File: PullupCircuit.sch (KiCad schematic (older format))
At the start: 4 parts, among them U4 DMC2700

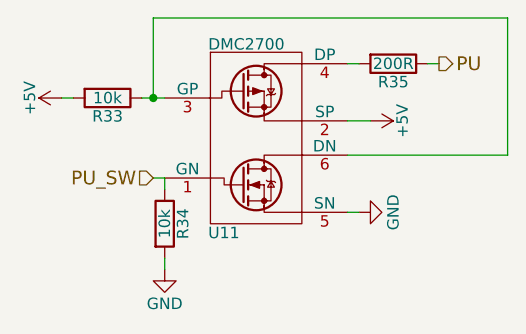
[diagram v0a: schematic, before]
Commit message: Fixed some annotations and footprints
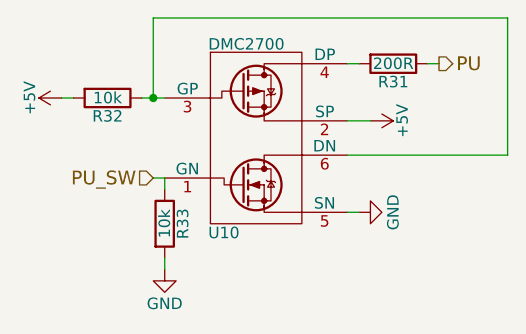
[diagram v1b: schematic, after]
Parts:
- renumbered R16 to R12, R14 to R13, R15 to R14, U4 to U3
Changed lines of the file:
@@
 $EndDescr
 $Comp
-L DMC2700 U4
+L DMC2700 U3
 U 1 1 59B3FFA1
 P 5200 2550
-AR Path="/59A988EA/59B40F2D/59B3FFA1" Ref="U4"  Part="1"
-AR Path="/59A988EA/59B419E1/59B3FFA1" Ref="U5"  Part="1"
-AR Path="/59B431E3/59B40F2D/59B3FFA1" Ref="U7"  Part="1"
-AR Path="/59B431E3/59B419E1/59B3FFA1" Ref="U8"  Part="1"
-AR Path="/59B46FD6/59B40F2D/59B3FFA1" Ref="U10"  Part="1"
-AR Path="/59B46FD6/59B419E1/59B3FFA1" Ref="U11"  Part="1"
-F 0 "U11" H 4990 2110 50  0000 L CNN
+AR Path="/59A988EA/59B40F2D/59B3FFA1" Ref="U3"  Part="1"
+AR Path="/59A988EA/59B419E1/59B3FFA1" Ref="U4"  Part="1"
+AR Path="/59B431E3/59B40F2D/59B3FFA1" Ref="U6"  Part="1"
+AR Path="/59B431E3/59B419E1/59B3FFA1" Ref="U7"  Part="1"
+AR Path="/59B46FD6/59B40F2D/59B3FFA1" Ref="U9"  Part="1"
+AR Path="/59B46FD6/59B419E1/59B3FFA1" Ref="U10"  Part="1"
+F 0 "U10" H 4990 2110 50  0000 L CNN
 F 1 "DMC2700" H 4990 2935 50  0000 L CNN
 F 2 "TO_SOT_Packages_SMD:SOT-23-6_Handsoldering" H 5450 2475 50  0001 L CIN
@@
 	5600 2500 5700 2500
 $Comp
-L R R16
+L R R12
 U 1 1 59B4002B
 P 5800 2250
-AR Path="/59A988EA/59B40F2D/59B4002B" Ref="R16"  Part="1"
-AR Path="/59A988EA/59B419E1/59B4002B" Ref="R19"  Part="1"
-AR Path="/59B431E3/59B40F2D/59B4002B" Ref="R24"  Part="1"
-AR Path="/59B431E3/59B419E1/59B4002B" Ref="R27"  Part="1"
-AR Path="/59B46FD6/59B40F2D/59B4002B" Ref="R32"  Part="1"
-AR Path="/59B46FD6/59B419E1/59B4002B" Ref="R35"  Part="1"
-F 0 "R35" V 5880 2250 50  0000 C CNN
+AR Path="/59A988EA/59B40F2D/59B4002B" Ref="R12"  Part="1"
+AR Path="/59A988EA/59B419E1/59B4002B" Ref="R15"  Part="1"
+AR Path="/59B431E3/59B40F2D/59B4002B" Ref="R20"  Part="1"
+AR Path="/59B431E3/59B419E1/59B4002B" Ref="R23"  Part="1"
+AR Path="/59B46FD6/59B40F2D/59B4002B" Ref="R28"  Part="1"
+AR Path="/59B46FD6/59B419E1/59B4002B" Ref="R31"  Part="1"
+F 0 "R31" V 5880 2250 50  0000 C CNN
 F 1 "200R" V 5800 2250 50  0000 C CNN
 F 2 "Resistors_SMD:R_1206_HandSoldering" V 5730 2250 50  0001 C CNN
@@
 	6000 2250 5950 2250
 $Comp
-L +5V #PWR044
+L +5V #PWR042
 U 1 1 59B40098
 P 5700 2500
-AR Path="/59A988EA/59B40F2D/59B40098" Ref="#PWR044"  Part="1"
-AR Path="/59A988EA/59B419E1/59B40098" Ref="#PWR048"  Part="1"
-AR Path="/59B431E3/59B40F2D/59B40098" Ref="#PWR070"  Part="1"
-AR Path="/59B431E3/59B419E1/59B40098" Ref="#PWR074"  Part="1"
-AR Path="/59B46FD6/59B40F2D/59B40098" Ref="#PWR096"  Part="1"
-AR Path="/59B46FD6/59B419E1/59B40098" Ref="#PWR0100"  Part="1"
-F 0 "#PWR0100" H 5700 2350 50  0001 C CNN
+AR Path="/59A988EA/59B40F2D/59B40098" Ref="#PWR042"  Part="1"
+AR Path="/59A988EA/59B419E1/59B40098" Ref="#PWR046"  Part="1"
+AR Path="/59B431E3/59B40F2D/59B40098" Ref="#PWR066"  Part="1"
+AR Path="/59B431E3/59B419E1/59B40098" Ref="#PWR070"  Part="1"
+AR Path="/59B46FD6/59B40F2D/59B40098" Ref="#PWR090"  Part="1"
+AR Path="/59B46FD6/59B419E1/59B40098" Ref="#PWR094"  Part="1"
+F 0 "#PWR094" H 5700 2350 50  0001 C CNN
 F 1 "+5V" H 5700 2640 50  0000 C CNN
 F 2 "" H 5700 2500 50  0001 C CNN
@@
 $EndComp
 $Comp
-L GND #PWR045
+L GND #PWR043
 U 1 1 59B400B7
 P 5650 2900
-AR Path="/59A988EA/59B40F2D/59B400B7" Ref="#PWR045"  Part="1"
-AR Path="/59A988EA/59B419E1/59B400B7" Ref="#PWR049"  Part="1"
-AR Path="/59B431E3/59B40F2D/59B400B7" Ref="#PWR071"  Part="1"
-AR Path="/59B431E3/59B419E1/59B400B7" Ref="#PWR075"  Part="1"
-AR Path="/59B46FD6/59B40F2D/59B400B7" Ref="#PWR097"  Part="1"
-AR Path="/59B46FD6/59B419E1/59B400B7" Ref="#PWR0101"  Part="1"
-F 0 "#PWR0101" H 5650 2650 50  0001 C CNN
+AR Path="/59A988EA/59B40F2D/59B400B7" Ref="#PWR043"  Part="1"
+AR Path="/59A988EA/59B419E1/59B400B7" Ref="#PWR047"  Part="1"
+AR Path="/59B431E3/59B40F2D/59B400B7" Ref="#PWR067"  Part="1"
+AR Path="/59B431E3/59B419E1/59B400B7" Ref="#PWR071"  Part="1"
+AR Path="/59B46FD6/59B40F2D/59B400B7" Ref="#PWR091"  Part="1"
+AR Path="/59B46FD6/59B419E1/59B400B7" Ref="#PWR095"  Part="1"
+F 0 "#PWR095" H 5650 2650 50  0001 C CNN
 F 1 "GND" H 5650 2750 50  0000 C CNN
 F 2 "" H 5650 2900 50  0001 C CNN
@@
 	4700 2400 4800 2400
 $Comp
-L R R14
+L R R13
 U 1 1 59B400E4
 P 4550 2400
-AR Path="/59A988EA/59B40F2D/59B400E4" Ref="R14"  Part="1"
-AR Path="/59A988EA/59B419E1/59B400E4" Ref="R17"  Part="1"
-AR Path="/59B431E3/59B40F2D/59B400E4" Ref="R22"  Part="1"
-AR Path="/59B431E3/59B419E1/59B400E4" Ref="R25"  Part="1"
-AR Path="/59B46FD6/59B40F2D/59B400E4" Ref="R30"  Part="1"
-AR Path="/59B46FD6/59B419E1/59B400E4" Ref="R33"  Part="1"
-F 0 "R33" V 4630 2400 50  0000 C CNN
+AR Path="/59A988EA/59B40F2D/59B400E4" Ref="R13"  Part="1"
+AR Path="/59A988EA/59B419E1/59B400E4" Ref="R16"  Part="1"
+AR Path="/59B431E3/59B40F2D/59B400E4" Ref="R21"  Part="1"
+AR Path="/59B431E3/59B419E1/59B400E4" Ref="R24"  Part="1"
+AR Path="/59B46FD6/59B40F2D/59B400E4" Ref="R29"  Part="1"
+AR Path="/59B46FD6/59B419E1/59B400E4" Ref="R32"  Part="1"
+F 0 "R32" V 4630 2400 50  0000 C CNN
 F 1 "10k" V 4550 2400 50  0000 C CNN
 F 2 "Resistors_SMD:R_0603_HandSoldering" V 4480 2400 50  0001 C CNN
@@
 Connection ~ 4750 2400
 $Comp
-L +5V #PWR046
+L +5V #PWR044
 U 1 1 59B4011D
 P 4350 2400
-AR Path="/59A988EA/59B40F2D/59B4011D" Ref="#PWR046"  Part="1"
-AR Path="/59A988EA/59B419E1/59B4011D" Ref="#PWR050"  Part="1"
-AR Path="/59B431E3/59B40F2D/59B4011D" Ref="#PWR072"  Part="1"
-AR Path="/59B431E3/59B419E1/59B4011D" Ref="#PWR076"  Part="1"
-AR Path="/59B46FD6/59B40F2D/59B4011D" Ref="#PWR098"  Part="1"
-AR Path="/59B46FD6/59B419E1/59B4011D" Ref="#PWR0102"  Part="1"
-F 0 "#PWR0102" H 4350 2250 50  0001 C CNN
+AR Path="/59A988EA/59B40F2D/59B4011D" Ref="#PWR044"  Part="1"
+AR Path="/59A988EA/59B419E1/59B4011D" Ref="#PWR048"  Part="1"
+AR Path="/59B431E3/59B40F2D/59B4011D" Ref="#PWR068"  Part="1"
+AR Path="/59B431E3/59B419E1/59B4011D" Ref="#PWR072"  Part="1"
+AR Path="/59B46FD6/59B40F2D/59B4011D" Ref="#PWR092"  Part="1"
+AR Path="/59B46FD6/59B419E1/59B4011D" Ref="#PWR096"  Part="1"
+F 0 "#PWR096" H 4350 2250 50  0001 C CNN
 F 1 "+5V" H 4350 2540 50  0000 C CNN
 F 2 "" H 4350 2400 50  0001 C CNN
@@
 	4400 2400 4350 2400
 $Comp
-L R R15
+L R R14
 U 1 1 59B4013F
 P 4800 2950
-AR Path="/59A988EA/59B40F2D/59B4013F" Ref="R15"  Part="1"
-AR Path="/59A988EA/59B419E1/59B4013F" Ref="R18"  Part="1"
-AR Path="/59B431E3/59B40F2D/59B4013F" Ref="R23"  Part="1"
-AR Path="/59B431E3/59B419E1/59B4013F" Ref="R26"  Part="1"
-AR Path="/59B46FD6/59B40F2D/59B4013F" Ref="R31"  Part="1"
-AR Path="/59B46FD6/59B419E1/59B4013F" Ref="R34"  Part="1"
-F 0 "R34" V 4880 2950 50  0000 C CNN
+AR Path="/59A988EA/59B40F2D/59B4013F" Ref="R14"  Part="1"
+AR Path="/59A988EA/59B419E1/59B4013F" Ref="R17"  Part="1"
+AR Path="/59B431E3/59B40F2D/59B4013F" Ref="R22"  Part="1"
+AR Path="/59B431E3/59B419E1/59B4013F" Ref="R25"  Part="1"
+AR Path="/59B46FD6/59B40F2D/59B4013F" Ref="R30"  Part="1"
+AR Path="/59B46FD6/59B419E1/59B4013F" Ref="R33"  Part="1"
+F 0 "R33" V 4880 2950 50  0000 C CNN
 F 1 "10k" V 4800 2950 50  0000 C CNN
 F 2 "Resistors_SMD:R_0603_HandSoldering" V 4730 2950 50  0001 C CNN
@@
 	4800 3100 4800 3150
 $Comp
-L GND #PWR047
+L GND #PWR045
 U 1 1 59B401E2
 P 4800 3150
-AR Path="/59A988EA/59B40F2D/59B401E2" Ref="#PWR047"  Part="1"
-AR Path="/59A988EA/59B419E1/59B401E2" Ref="#PWR051"  Part="1"
-AR Path="/59B431E3/59B40F2D/59B401E2" Ref="#PWR073"  Part="1"
-AR Path="/59B431E3/59B419E1/59B401E2" Ref="#PWR077"  Part="1"
-AR Path="/59B46FD6/59B40F2D/59B401E2" Ref="#PWR099"  Part="1"
-AR Path="/59B46FD6/59B419E1/59B401E2" Ref="#PWR0103"  Part="1"
-F 0 "#PWR0103" H 4800 2900 50  0001 C CNN
+AR Path="/59A988EA/59B40F2D/59B401E2" Ref="#PWR045"  Part="1"
+AR Path="/59A988EA/59B419E1/59B401E2" Ref="#PWR049"  Part="1"
+AR Path="/59B431E3/59B40F2D/59B401E2" Ref="#PWR069"  Part="1"
+AR Path="/59B431E3/59B419E1/59B401E2" Ref="#PWR073"  Part="1"
+AR Path="/59B46FD6/59B40F2D/59B401E2" Ref="#PWR093"  Part="1"
+AR Path="/59B46FD6/59B419E1/59B401E2" Ref="#PWR097"  Part="1"
+F 0 "#PWR097" H 4800 2900 50  0001 C CNN
 F 1 "GND" H 4800 3000 50  0000 C CNN
 F 2 "" H 4800 3150 50  0001 C CNN
